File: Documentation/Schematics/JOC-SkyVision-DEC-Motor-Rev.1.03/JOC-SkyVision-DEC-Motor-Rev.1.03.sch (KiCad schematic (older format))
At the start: 51 parts, among them J1 RJ45, J2 RJ45, J3 Unknown_Barrel_Connector, Q1 4947A Dual P-Channel Mosfet, Q2 4936A Dual N-Channel Mosfet, U1 PIC16F690-ISO, U2_LED Motor Encoder LED, U2_PD Motor Encoder Photodiodes, U3 AZ1117-5.0 (GH15E), U4 TC4426A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

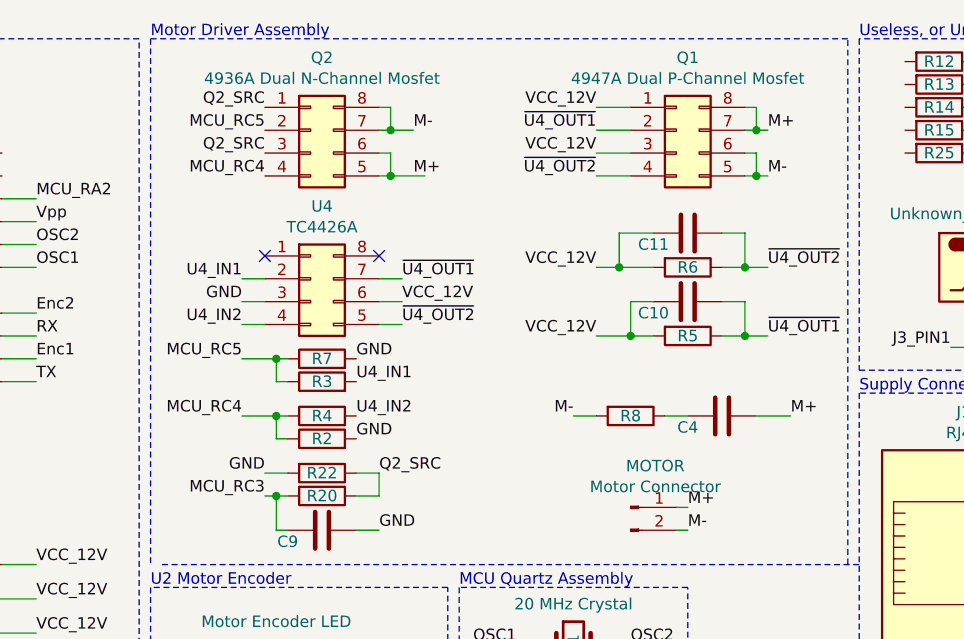
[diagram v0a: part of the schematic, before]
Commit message: Added RA Motor data sheets
updated DEC motor wrong polarity on mosfets :o
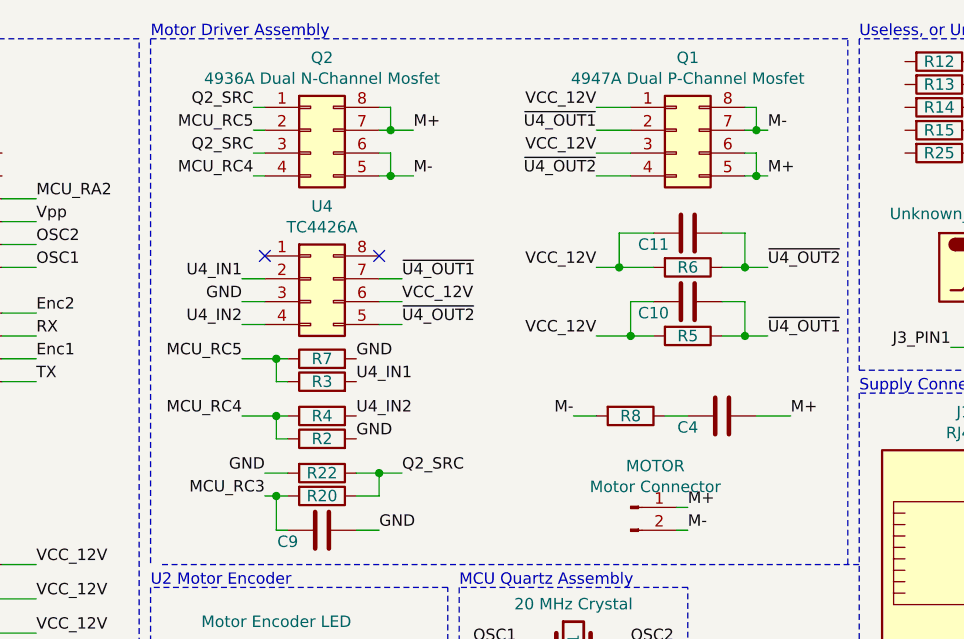
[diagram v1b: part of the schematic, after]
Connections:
- net M+: now also Q1.5 (Pin_5), Q1.6 (Pin_6), Q2.7 (Pin_7), Q2.8 (Pin_8); no longer Q1.7 (Pin_7), Q1.8 (Pin_8), Q2.5 (Pin_5), Q2.6 (Pin_6)
- net M-: now also Q1.7 (Pin_7), Q1.8 (Pin_8), Q2.5 (Pin_5), Q2.6 (Pin_6); no longer Q1.5 (Pin_5), Q1.6 (Pin_6), Q2.7 (Pin_7), Q2.8 (Pin_8)
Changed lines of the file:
@@
 Wire Wire Line
 	7200 2850 7250 2850
+Text Label 6050 1100 0    50   ~ 0
+M+
+Text Label 7600 1300 0    50   ~ 0
+M+
 Text Label 6050 1300 0    50   ~ 0
-M+
+M-
 Text Label 7600 1100 0    50   ~ 0
-M+
-Text Label 6050 1100 0    50   ~ 0
-M-
-Text Label 7600 1300 0    50   ~ 0
 M-
 Wire Wire Line
@@
 Connection ~ 5950 1300
 Wire Wire Line
-	5950 1300 6100 1300
+	5950 1300 6050 1300
 Text Label 5400 2600 2    50   ~ 0
 GND
@@
 Text Label 5300 1850 2    50   ~ 0
 GND
-Text Label 5400 1100 2    50   ~ 0
+Text Label 5350 1100 2    50   ~ 0
 MCU_RC5
-Text Label 5400 1300 2    50   ~ 0
+Text Label 5350 1300 2    50   ~ 0
 MCU_RC4
 Text Label 1150 1700 2    50   ~ 0
@@
 Wire Wire Line
 	5900 2600 5800 2600
-Text Label 5900 2600 0    50   ~ 0
+Text Label 6000 2600 0    50   ~ 0
 Q2_SRC
-Text Label 5400 1000 2    50   ~ 0
+Text Label 5350 1000 2    50   ~ 0
 Q2_SRC
-Text Label 5400 1200 2    50   ~ 0
+Text Label 5350 1200 2    50   ~ 0
 Q2_SRC
 Wire Notes Line
@@
 Text Notes 8000 700  0    50   ~ 0
 Useless, or Unknown
+Wire Wire Line
+	5350 1000 5400 1000
+Wire Wire Line
+	5350 1100 5400 1100
+Wire Wire Line
+	5350 1200 5400 1200
+Wire Wire Line
+	5350 1300 5400 1300
+Wire Wire Line
+	5900 2600 6000 2600
+Connection ~ 5900 2600
 $EndSCHEMATC

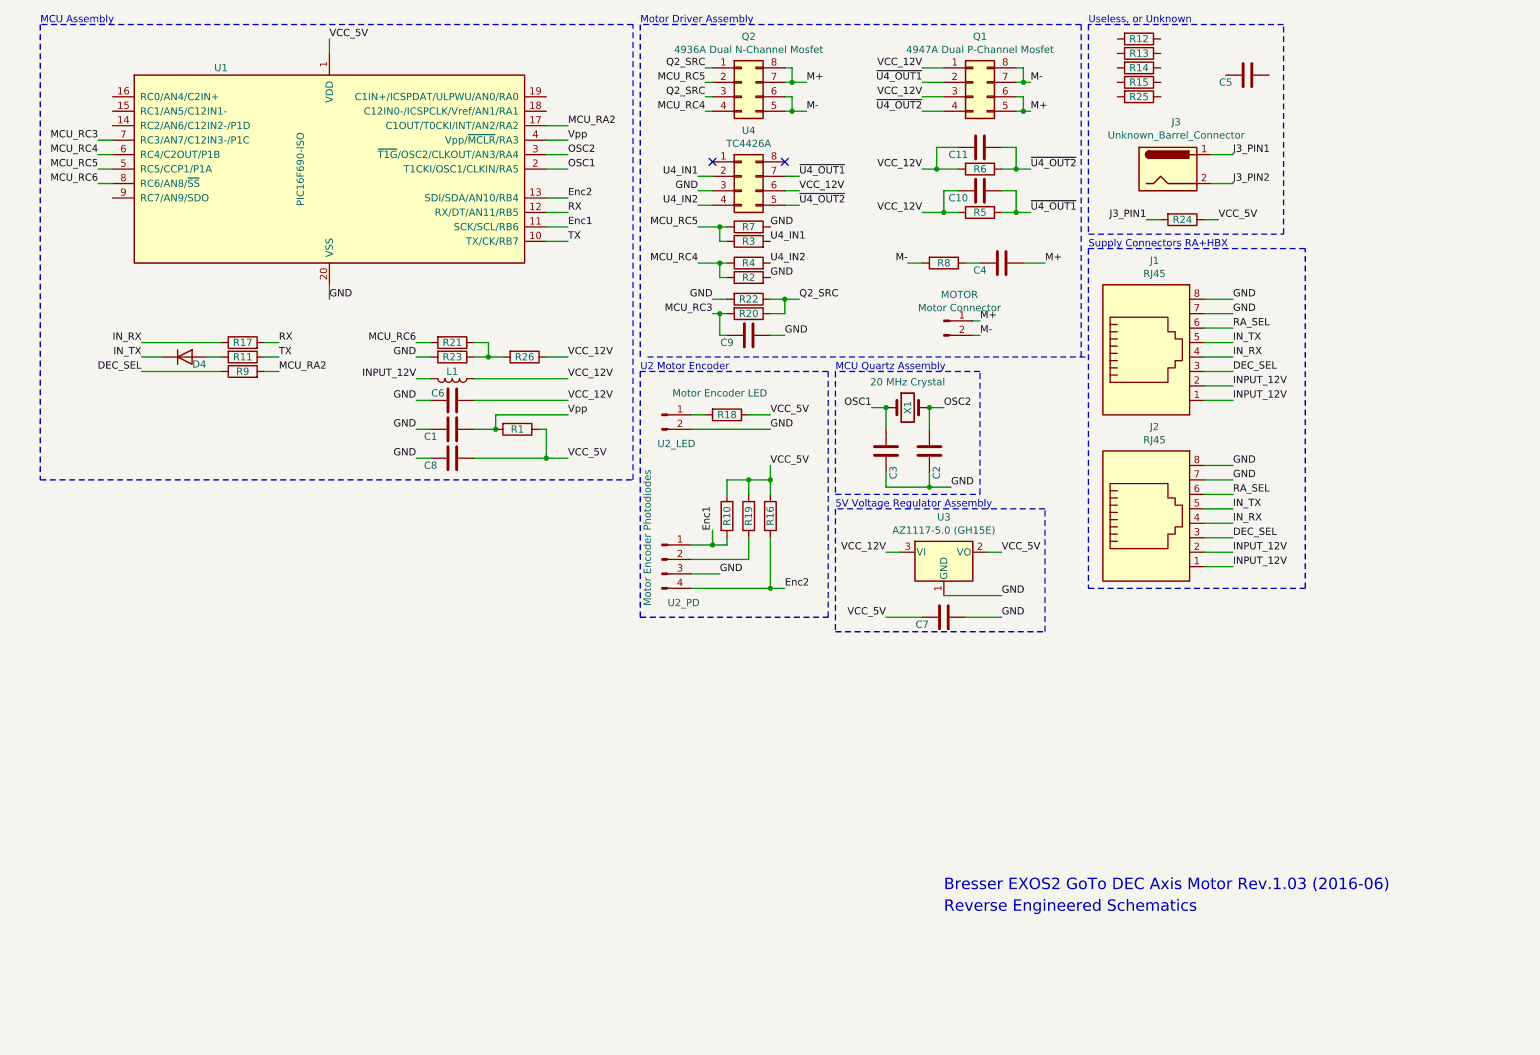
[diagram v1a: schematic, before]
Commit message: updated schematics
added introduction text for schematics
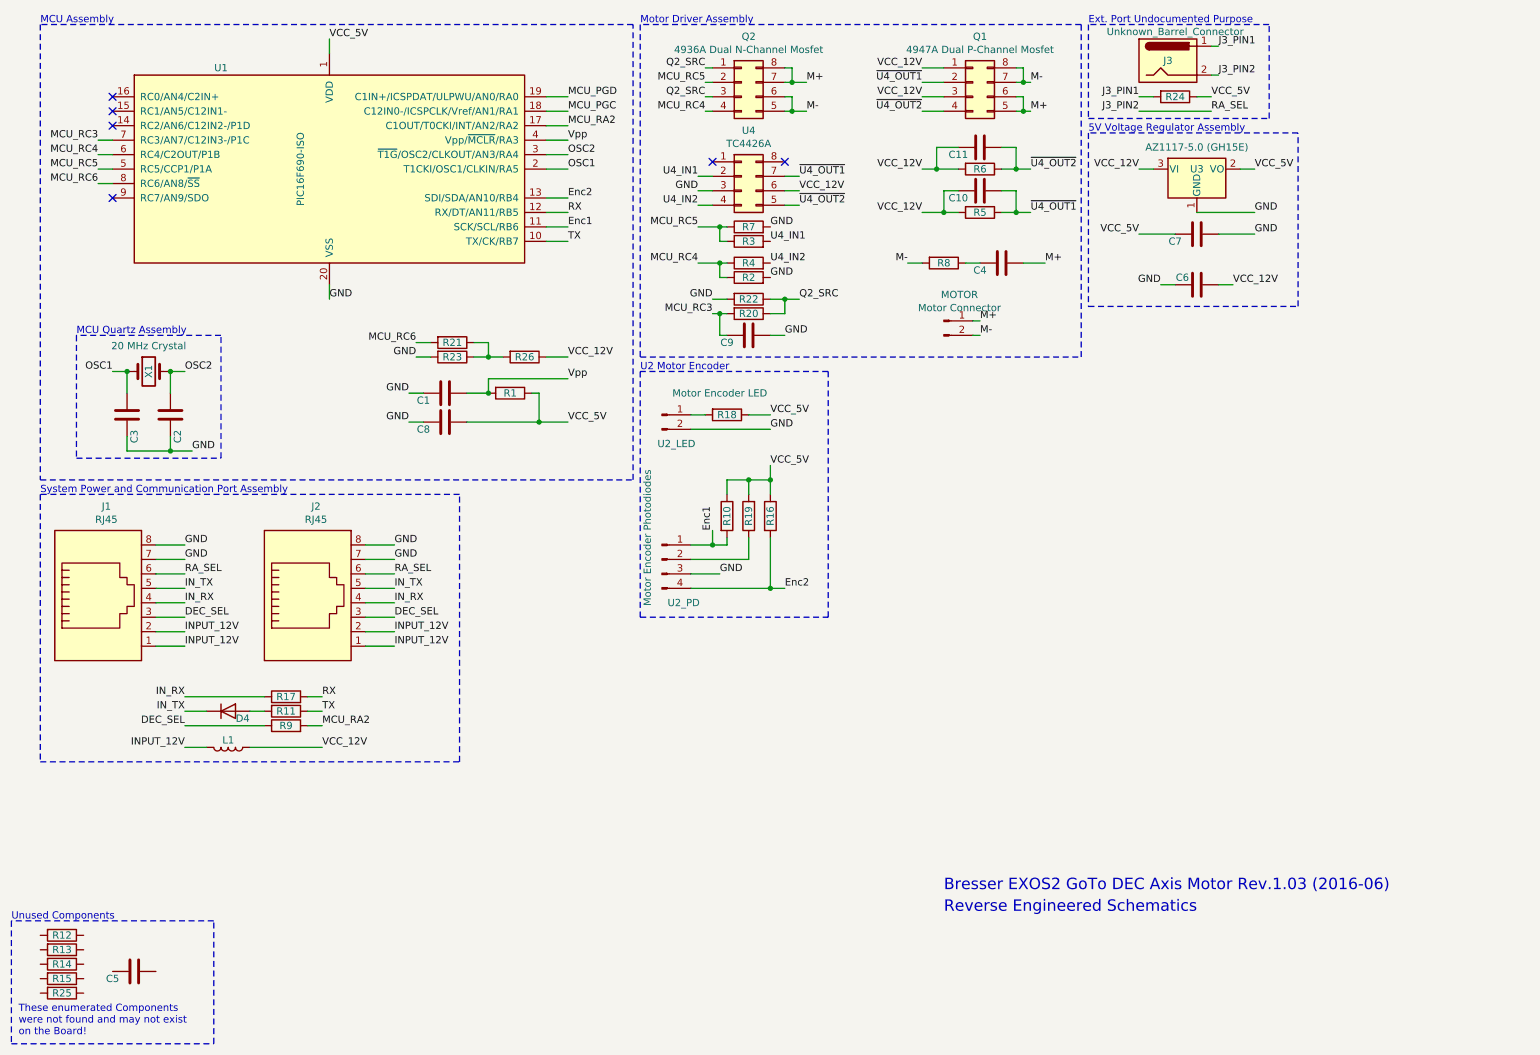
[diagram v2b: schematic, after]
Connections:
- net RA_SEL is gone; now on net J3_PIN2: J1.6, J2.6
- net MCU_PGC: now reaches U1.18 (C12IN0-/ICSPCLK/Vref/AN1/RA1)
- net MCU_PGD: now reaches U1.19 (C1IN+/ICSPDAT/ULPWU/AN0/RA0)
- no-connect marks 2 -> 6
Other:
- note added: "Ext. Port Undocumented Purpose"
- note added: "System Power and Communication Port Assembly"
- note added: "These enumerated Components\nwere not found and may not exist\non the Board!"
- note added: "Unused Components"
- note removed: "Supply Connectors RA+HBX"
- note removed: "Useless, or Unknown"
- moved on the sheet: C1, C2, C3, C5, C6, C7, C8, D4, J1, J2, J3, L1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
